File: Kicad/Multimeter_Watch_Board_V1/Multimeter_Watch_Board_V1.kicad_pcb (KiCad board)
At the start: 4 copper layers, 55 x 46 mm, 34 parts, among them J1 AudioJack3_Ground_renamedPins, J2 AudioJack3_Ground_renamedPins, J3 AudioJack3_Ground_renamedPins, J4 Conn_01x16_Female, J5 Conn_01x16_Female, U1 PCF85163-SO08, U2 AD8592, Y1 32kHz

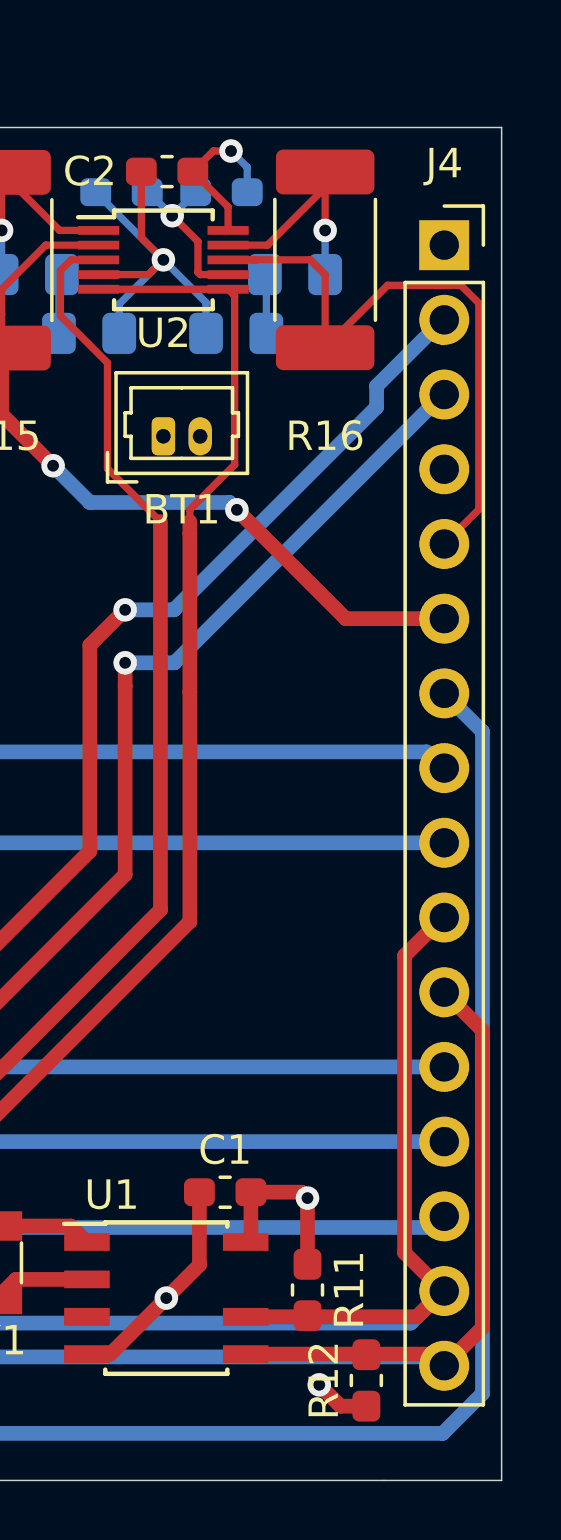
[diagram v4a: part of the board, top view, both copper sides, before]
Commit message: measure header distance by center of hole (courtyards are not symmetrical)
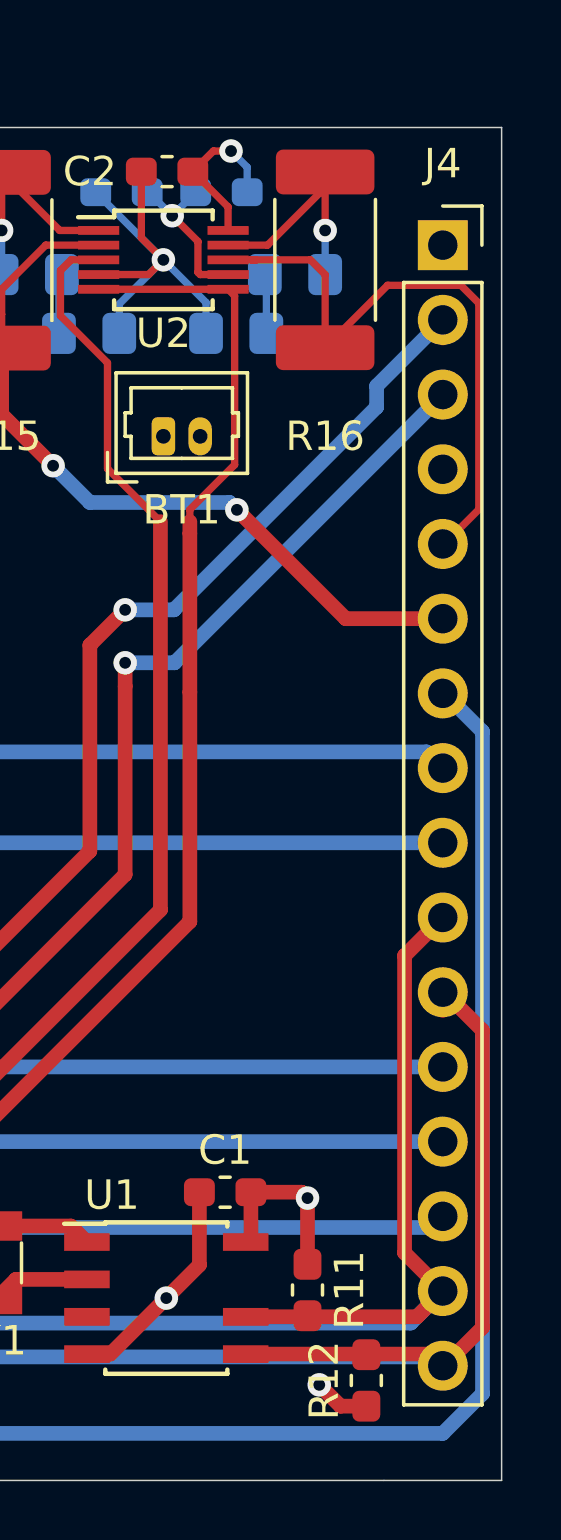
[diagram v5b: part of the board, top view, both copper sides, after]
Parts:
- moved J4 0.05 mm to (153.0, 54.0)

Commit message: move I2C pullups from VCC to enable
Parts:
- moved R12 13.3 mm to (148.0, 79.5), turned to 0 degrees
- moved R11 13.0 mm to (148.0, 76.5), turned to 0 degrees
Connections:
- J4 pad 10: /SCL -> /SDA
- J4 pad 11: /SDA -> /SCL
- R11 pad 1: /VCC -> /PD3
- R11 pad 2: /SCL -> /SDA
- R12 pad 1: /VCC -> /PD3
- R12 pad 2: /SDA -> /SCL
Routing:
- net /SDA: track 71.5 -> 77.7 mm
- net /PD3: track 83.4 -> 89.5 mm
- net /VCC: track 17.8 -> 13.6 mm, vias 4 -> 3
- net /SCL: track 69.7 -> 71.3 mm

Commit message: display board done, todo: move display down to allow for jack labels
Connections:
- J4 pad 10: /SDA -> /SCL
- J4 pad 11: /SCL -> /SDA
- R11 pad 2: /SDA -> /SCL
- R12 pad 2: /SCL -> /SDA

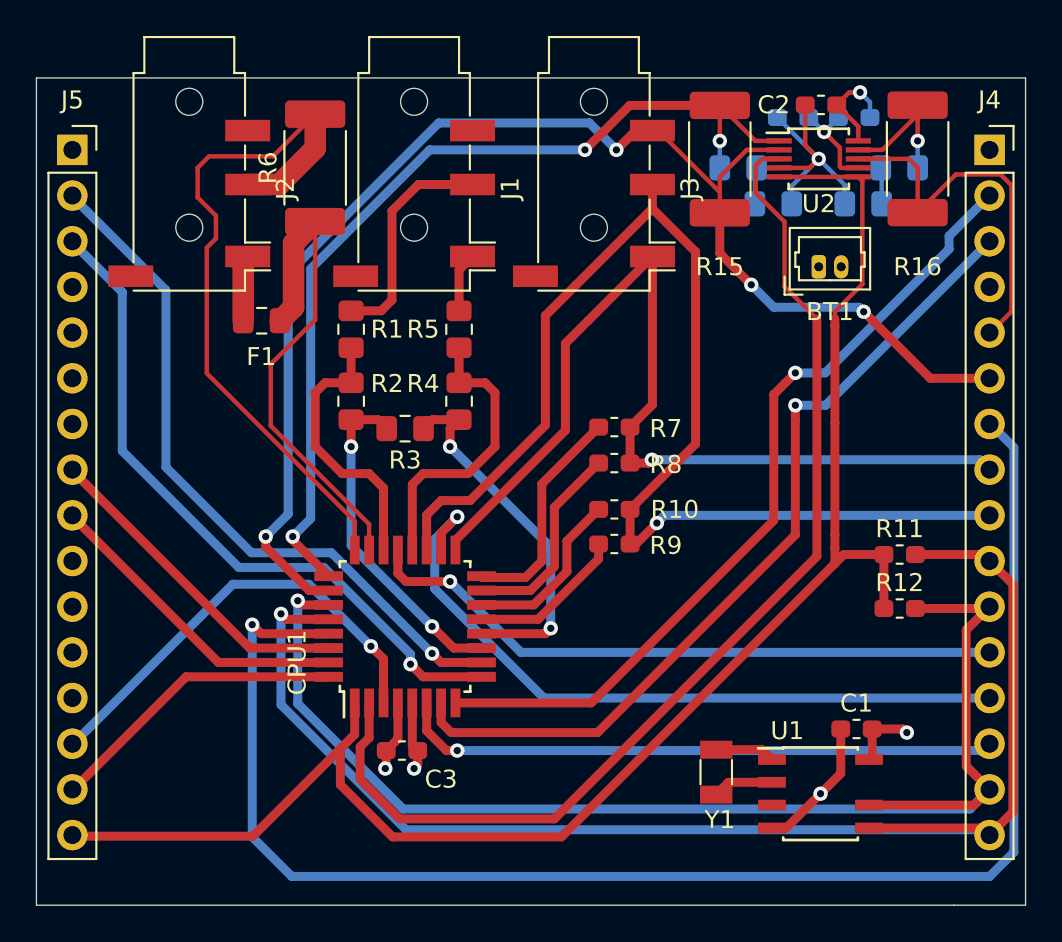
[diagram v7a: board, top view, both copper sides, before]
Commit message: Add more decoupling and filtering capacitors; add series resistors for Serial port. Minor improvements.
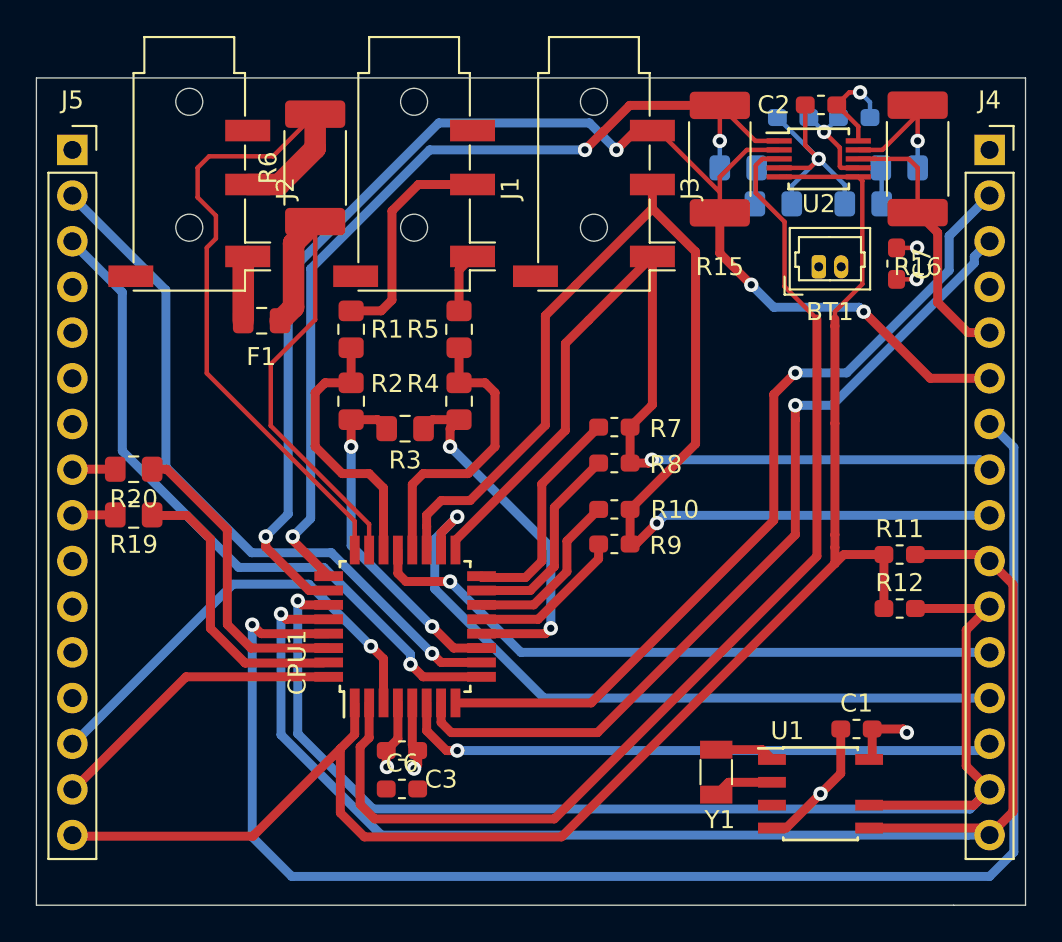
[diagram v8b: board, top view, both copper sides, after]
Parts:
- added C6: 10n, Capacitor_SMD:C_0603_1608Metric_Pad1.05x0.95mm_HandSolder, F.Cu at (120.3, 89.5)
- added C7: 10u, Capacitor_SMD:C_0603_1608Metric_Pad1.05x0.95mm_HandSolder, F.Cu at (147.8, 60.3)
- added R19: 1k, Resistor_SMD:R_0805_2012Metric_Pad1.15x1.40mm_HandSolder, F.Cu at (105.4, 74.3)
- added R20: 1k, Resistor_SMD:R_0805_2012Metric_Pad1.15x1.40mm_HandSolder, F.Cu at (105.4, 71.8)
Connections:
- CPU1 pad 30: /D0 -> Net-(CPU1-Pad30)
- CPU1 pad 31: /D1 -> Net-(CPU1-Pad31)
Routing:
- net Net-(CPU1-Pad30): track 0.00 -> 17.0 mm
- net Net-(CPU1-Pad31): track 0.00 -> 16.1 mm
- net /D0: track 18.3 -> 2.40 mm
- net /D1: track 17.6 -> 2.40 mm
- net /VCC_HALF: track 21.8 -> 15.8 mm
- net /GND: track 26.6 -> 27.7 mm, vias 3 -> 4
- net /VCC: track 13.6 -> 14.7 mm, vias 3 -> 4
- net /SDA: track 77.7 -> 78.7 mm
- net /SCL: track 71.3 -> 72.3 mm
- net /PD3: track 89.5 -> 90.4 mm
- net /PD4: track 61.4 -> 62.2 mm
- net /PB7: track 46.5 -> 47.2 mm
